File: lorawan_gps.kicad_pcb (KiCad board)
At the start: 2 copper layers, 75 x 20 mm, 60 parts, among them IC1 TPS61201, P1 BL_PAD, P10 CONN_01X01, P11 CONN_01X04, P2 SWD_DAT, P3 SWD_CLK, P4 SWD_3V3, P5 SWD_GND, P6 SWD_RST, P8 CONN_01X01, P9 CONN_01X01, SW1 SW_PUSH, SW2 SW_PUSH, U1 SHT21, U2 MPU-9250, U3 RFM9xW, U4 SAMD21E17A, U5 MAX-M8, Y1 32.768kHz

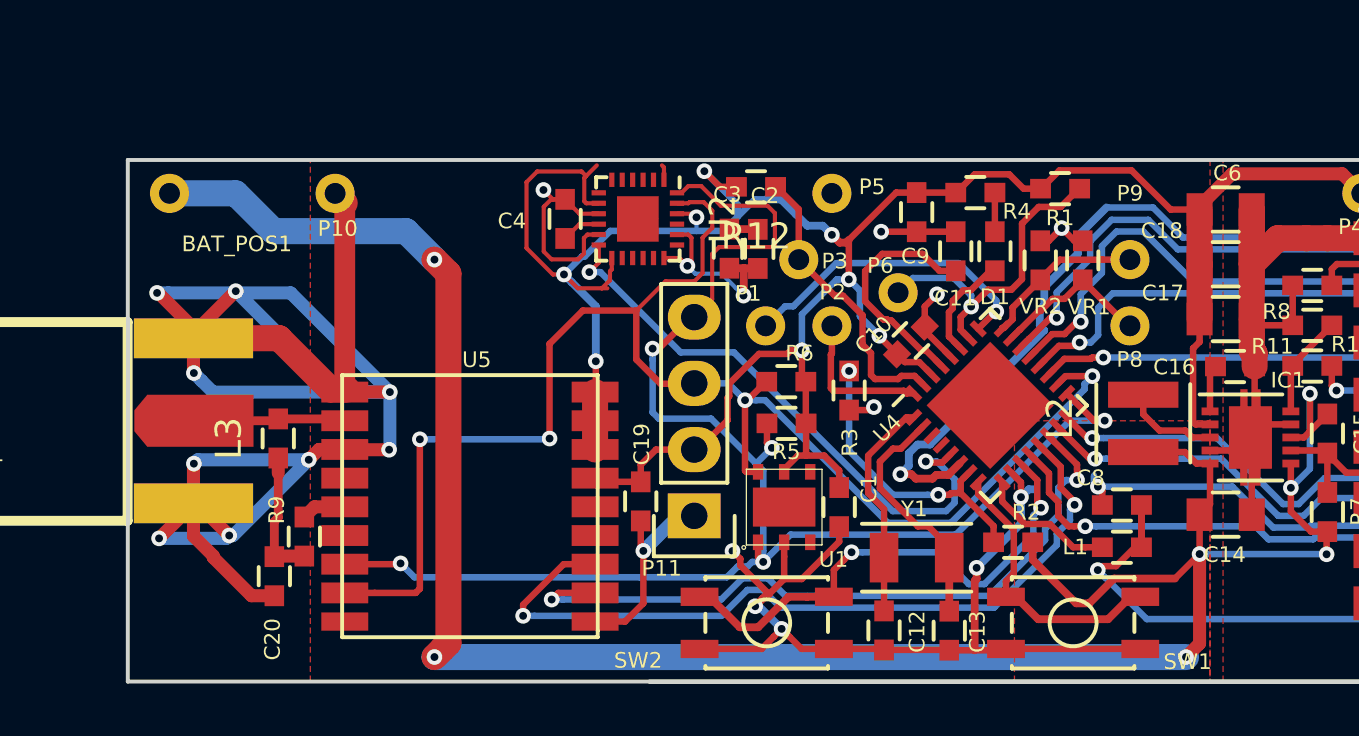
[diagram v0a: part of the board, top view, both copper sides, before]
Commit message: Started work to add the power mux and USB connector
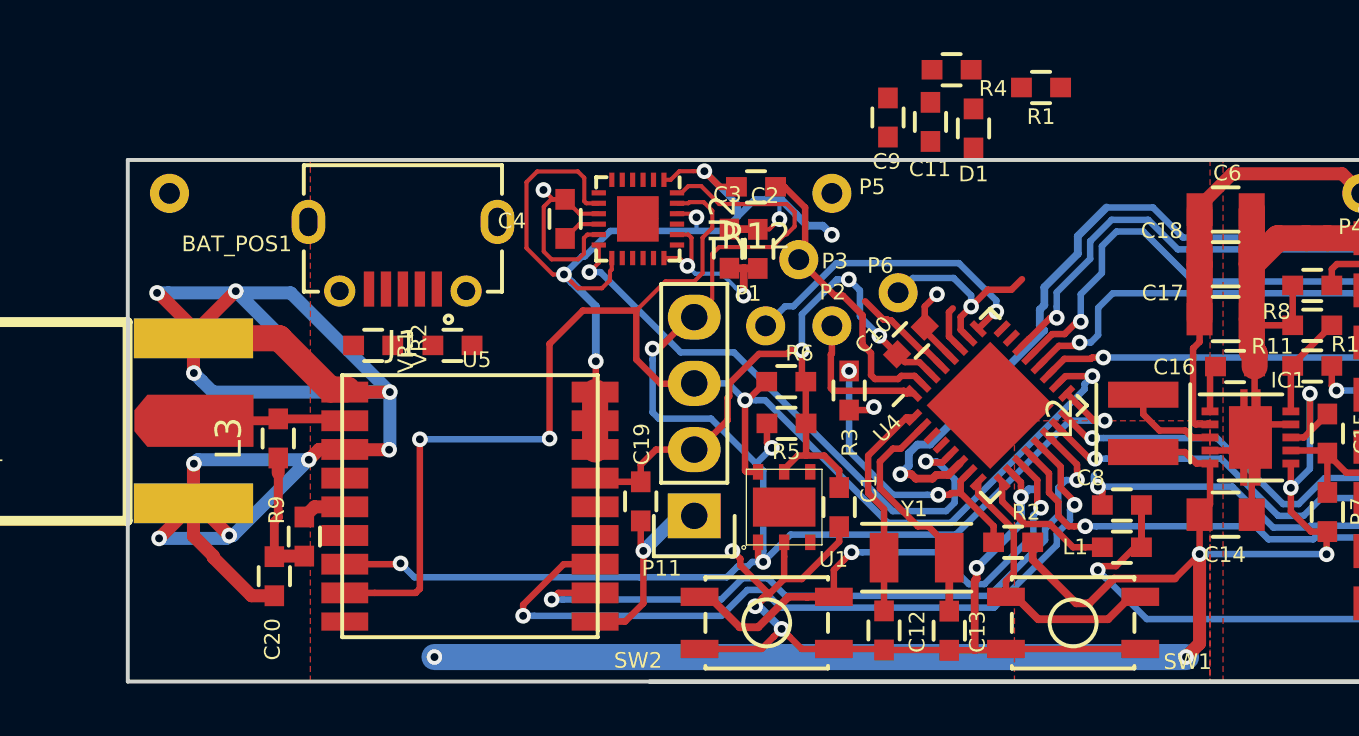
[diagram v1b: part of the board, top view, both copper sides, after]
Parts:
- removed P10, P8, P9: CONN_01X01, Measurement_Points:Measurement_Point_Round-TH_Small
- added J1: MICRO-USB, RocketScreamKicadLibrary:MICRO-USB, F.Cu at (115.5, 73.5)
- moved VR2 25.8 mm to (114.4, 77.1), turned to 180 degrees
- moved VR1 24.4 mm to (117.5, 77.1), turned to 0 degrees
- moved C11 5.05 mm to (135.8, 68.5)
- moved R4 4.80 mm to (136.6, 66.5)
- moved D1 4.78 mm to (137.4, 68.8)
- moved R1 3.95 mm to (140.0, 67.2)
- moved C9 3.79 mm to (134.2, 68.4)
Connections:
- net Net-(P8-Pad1) renamed /MCU/Data-
- net Net-(P9-Pad1) renamed /MCU/Data+
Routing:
- net /Battery/V_BAT: track 91.3 -> 64.4 mm, vias 7 -> 6
- net +3V3: track 162.6 -> 146.5 mm, vias 12 -> 13
- net GND: track 228.3 -> 215.7 mm, vias 28 -> 26
- net /MCU/Data+: track 6.30 -> 0.00 mm
- net /MCU/Data-: track 6.25 -> 0.00 mm
- net Net-(C11-Pad1): track 9.12 -> 3.95 mm
- net /MCU/#RESET: track 12.5 -> 7.63 mm
- net Net-(D1-Pad1): track 4.11 -> 1.73 mm
- net Net-(D1-Pad2): track 1.51 -> 0.00 mm
- net /MCU/MPU_SDA: track 60.8 -> 61.9 mm

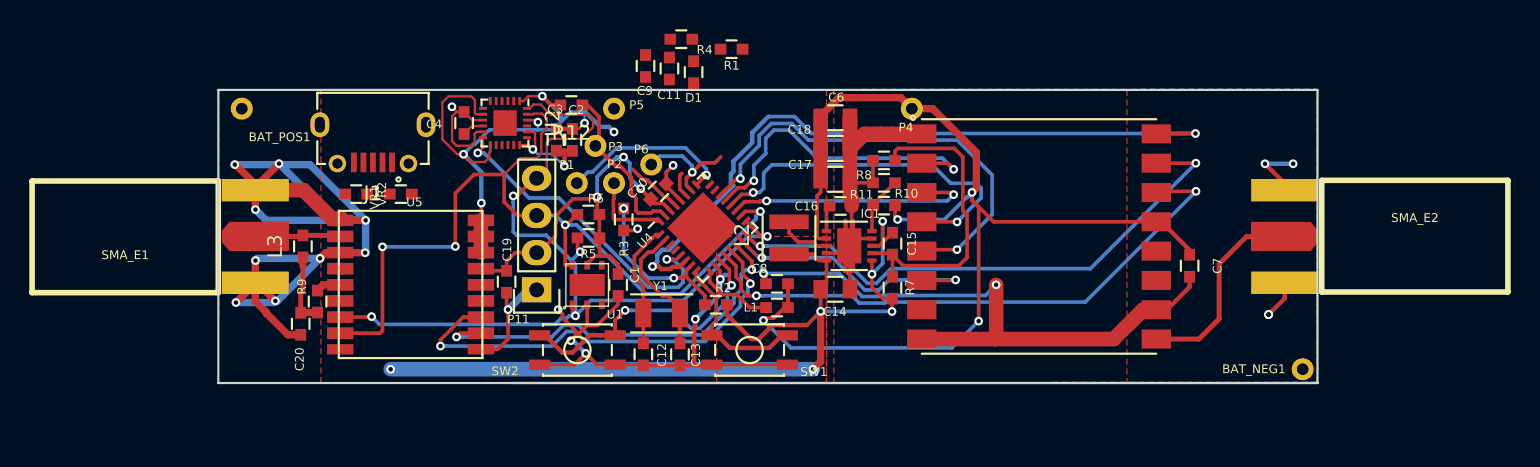
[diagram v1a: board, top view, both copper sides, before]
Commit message: Added USB connector, diode or etc to layout@
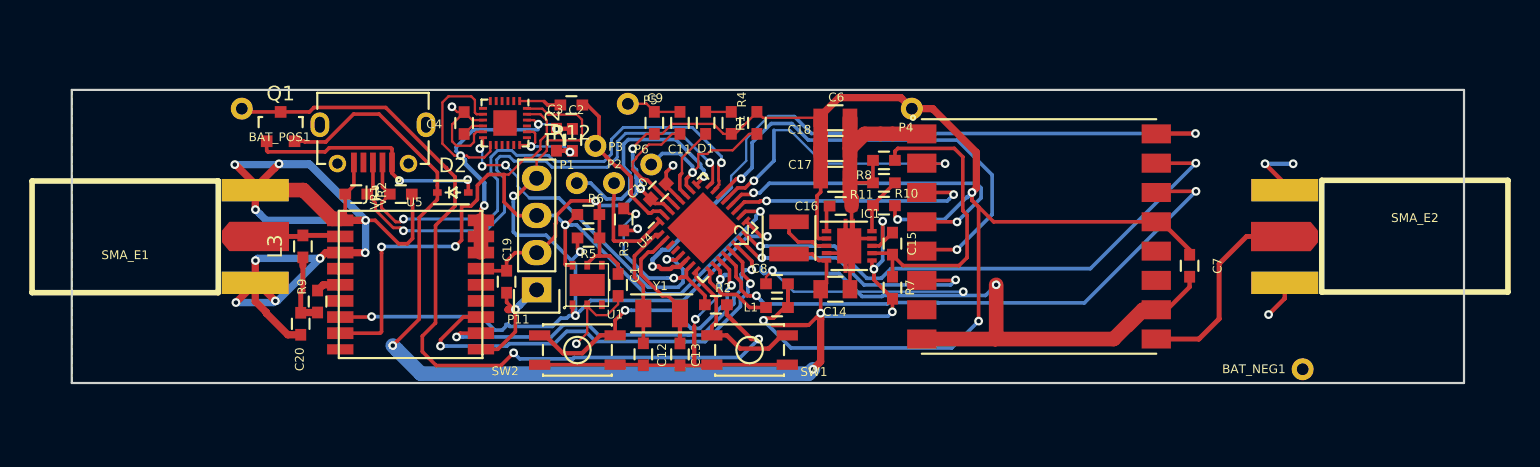
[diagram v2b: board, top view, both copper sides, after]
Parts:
- added D2: D_Schottky, Diodes_SMD:SOD-323, F.Cu at (121.0, 77.0)
- added Q1: Q_PMOS_GSD, TO_SOT_Packages_SMD:SOT-23, F.Cu at (109.2, 72.5)
- moved R4 6.65 mm to (140.0, 72.2), turned to 90 degrees
- moved R1 5.32 mm to (141.8, 72.2), turned to 270 degrees
- moved C9 3.93 mm to (134.8, 72.2), turned to 90 degrees
- moved C11 3.78 mm to (136.5, 72.2)
- moved D1 3.56 mm to (138.2, 72.2)
- moved P5 1.00 mm to (132.9, 71.0)
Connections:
- net /MCU/Data+ renamed /Battery and USB Connector/D+
- net /MCU/Data- renamed /Battery and USB Connector/D-
- BAT_POS1 pad 1: /Battery/V_BAT -> /Battery and USB Connector/V_BAT
- C14 pad 1: /Battery/V_BAT -> Net-(C14-Pad1)
- C15 pad 1: /Battery/V_BAT -> Net-(C14-Pad1)
- IC1 pad 5: /Battery/V_BAT -> Net-(C14-Pad1)
- IC1 pad 6: /Battery/V_BAT -> Net-(C14-Pad1)
- IC1 pad 8: /Battery/V_BAT -> Net-(C14-Pad1)
- J1 pad 4: Net-(J1-Pad4) -> (no net)
- J1 pad 6: GND -> (no net)
- J1 pad 7: GND -> (no net)
- J1 pad 8: GND -> (no net)
- J1 pad 9: GND -> (no net)
- L2 pad 1: /Battery/V_BAT -> Net-(C14-Pad1)
- R2 pad 1: /Battery/V_BAT -> /Battery and USB Connector/V_BAT
- R7 pad 1: /Battery/V_BAT -> Net-(C14-Pad1)
- U1 pad 3: Net-(U1-Pad3) -> (no net)
- U1 pad 4: Net-(U1-Pad4) -> (no net)
- U2 pad 14: Net-(U2-Pad14) -> (no net)
- U2 pad 15: Net-(U2-Pad15) -> (no net)
- U2 pad 16: Net-(U2-Pad16) -> (no net)
- U2 pad 17: Net-(U2-Pad17) -> (no net)
- U2 pad 19: Net-(U2-Pad19) -> (no net)
- U2 pad 2: Net-(U2-Pad2) -> (no net)
- U2 pad 21: Net-(U2-Pad21) -> (no net)
- U2 pad 3: Net-(U2-Pad3) -> (no net)
- U2 pad 4: Net-(U2-Pad4) -> (no net)
- U2 pad 5: Net-(U2-Pad5) -> (no net)
- U2 pad 6: Net-(U2-Pad6) -> (no net)
- U2 pad 7: Net-(U2-Pad7) -> (no net)
- U3 pad 11: Net-(U3-Pad11) -> (no net)
- U3 pad 12: Net-(U3-Pad12) -> (no net)
- U3 pad 7: Net-(U3-Pad7) -> (no net)
- U4 pad 3: Net-(U4-Pad3) -> (no net)
- U4 pad 4: Net-(U4-Pad4) -> (no net)
- U5 pad 13: Net-(U5-Pad13) -> (no net)
- U5 pad 15: Net-(U5-Pad15) -> (no net)
- U5 pad 18: Net-(U5-Pad18) -> (no net)
- U5 pad 4: Net-(U5-Pad4) -> (no net)
- U5 pad 5: Net-(U5-Pad5) -> (no net)
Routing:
- net Net-(C14-Pad1): track 0.00 -> 85.0 mm, vias 0 -> 6
- net /Battery/V_BAT: track 64.4 -> 0.00 mm, vias 6 -> 0
- net /Battery and USB Connector/V_BAT: track 0.00 -> 57.5 mm, vias 0 -> 2
- net /Battery and USB Connector/D-: track 0.00 -> 37.1 mm, vias 0 -> 2
- net /Battery and USB Connector/D+: track 0.00 -> 36.4 mm, vias 0 -> 2
- net GND: track 215.7 -> 239.8 mm, vias 26 -> 24
- net Net-(D2-Pad2): track 0.00 -> 17.3 mm, vias 0 -> 2
- net +3V3: track 146.5 -> 153.8 mm, vias 13 -> 11
- net Net-(C11-Pad1): track 3.95 -> 8.52 mm
- net /MCU/#RESET: track 7.63 -> 11.4 mm
- net Net-(P1-Pad1): track 11.8 -> 15.4 mm
- net Net-(D1-Pad1): track 1.73 -> 5.08 mm
- net Net-(P2-Pad1): track 5.66 -> 7.67 mm
- net Net-(D1-Pad2): track 0.00 -> 1.75 mm
- net /MCU/MPU_SCK: track 24.9 -> 23.3 mm
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- removed copper zone on F.Cu, net +3V3
- removed copper zone on F.Cu, net /Battery/V_BAT
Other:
- board size 75 x 20 mm -> 95 x 20 mm

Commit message: Added dielectric antennae, finished wiring, DRC pass, no unconnects
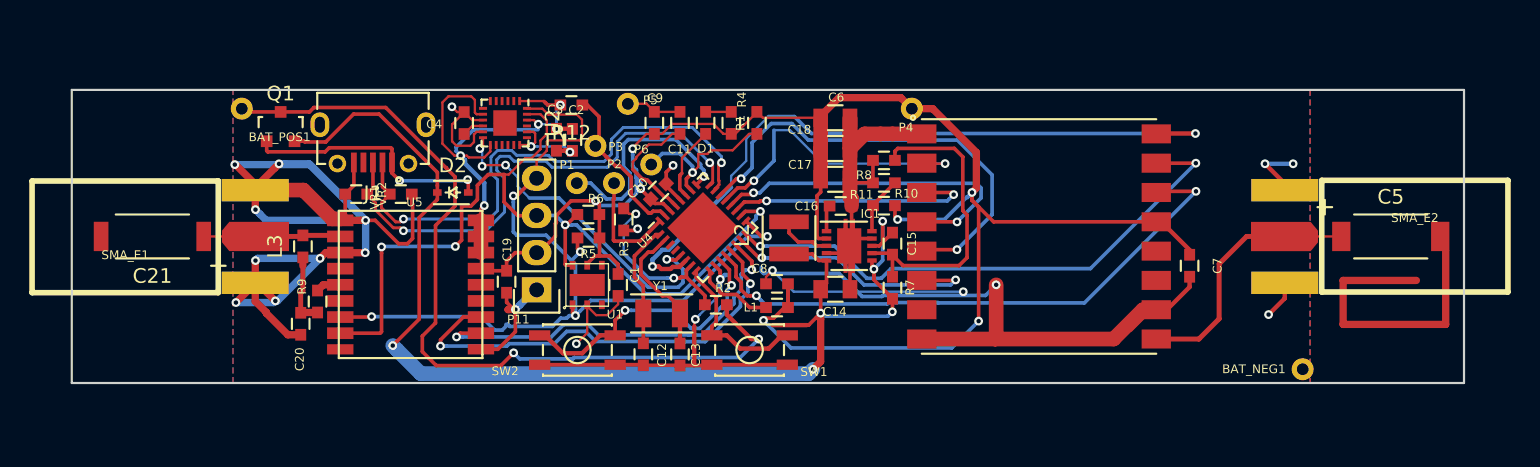
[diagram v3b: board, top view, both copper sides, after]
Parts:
- added C21: CP, Johanson:1575AT43A0040, F.Cu at (100.5, 80.0)
- added C5: CP, Johanson:0868AT43A0020, F.Cu at (185.0, 80.0)
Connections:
- J1 pad 4: (no net) -> Net-(J1-Pad4)
- J1 pad 6: (no net) -> Net-(J1-Pad6)
- J1 pad 7: (no net) -> Net-(J1-Pad7)
- J1 pad 8: (no net) -> Net-(J1-Pad8)
- J1 pad 9: (no net) -> Net-(J1-Pad9)
- U1 pad 3: (no net) -> Net-(U1-Pad3)
- U1 pad 4: (no net) -> Net-(U1-Pad4)
- U2 pad 14: (no net) -> Net-(U2-Pad14)
- U2 pad 15: (no net) -> Net-(U2-Pad15)
- U2 pad 16: (no net) -> Net-(U2-Pad16)
- U2 pad 17: (no net) -> Net-(U2-Pad17)
- U2 pad 19: (no net) -> Net-(U2-Pad19)
- U2 pad 2: (no net) -> Net-(U2-Pad2)
- U2 pad 21: (no net) -> Net-(U2-Pad21)
- U2 pad 3: (no net) -> Net-(U2-Pad3)
- U2 pad 4: (no net) -> Net-(U2-Pad4)
- U2 pad 5: (no net) -> Net-(U2-Pad5)
- U2 pad 6: (no net) -> Net-(U2-Pad6)
- U2 pad 7: (no net) -> Net-(U2-Pad7)
- U3 pad 11: (no net) -> Net-(U3-Pad11)
- U3 pad 12: (no net) -> Net-(U3-Pad12)
- U3 pad 7: (no net) -> Net-(U3-Pad7)
- U4 pad 3: (no net) -> Net-(U4-Pad3)
- U4 pad 4: (no net) -> Net-(U4-Pad4)
- U5 pad 13: (no net) -> Net-(U5-Pad13)
- U5 pad 15: (no net) -> Net-(U5-Pad15)
- U5 pad 18: (no net) -> Net-(U5-Pad18)
- U5 pad 4: (no net) -> Net-(U5-Pad4)
- U5 pad 5: (no net) -> Net-(U5-Pad5)
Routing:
- net Net-(C5-Pad1): track 15.9 -> 20.0 mm
- net +3V3: track 153.8 -> 157.6 mm, vias 11 -> 12
- net /GPS/GPS_FEEDER: track 7.88 -> 9.38 mm
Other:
- net class Default: clearance 0.2 -> 0.16; trace_width 0.25 -> 0.16
- rule trace_clearance: 0.2 -> 0.16

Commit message: Added USB monitoring resistors, still need to set values. Also added stitching vias and tried to clean up some layout
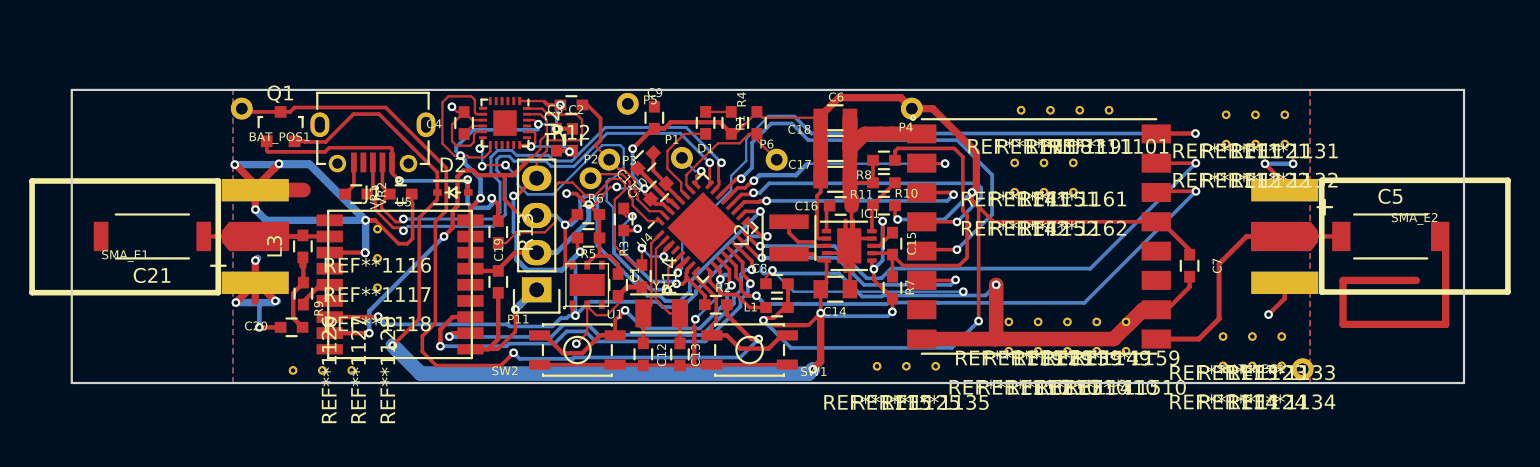
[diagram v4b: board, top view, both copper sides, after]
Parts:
- added R13: R, Capacitors_SMD:C_0603, F.Cu at (124.1, 79.7)
- added R14: R, Capacitors_SMD:C_0603, F.Cu at (133.9, 82.7)
- added REF**11101: Stitch_Via, Oddities:Stitch_Via, F.Cu at (165.8, 71.4)
- added REF**1111: Stitch_Via, Oddities:Stitch_Via, F.Cu at (173.8, 71.7)
- added REF**11110: Stitch_Via, Oddities:Stitch_Via, F.Cu at (158.9, 87.8)
- added REF**1112: Stitch_Via, Oddities:Stitch_Via, F.Cu at (173.8, 73.7)
- added REF**1113: Stitch_Via, Oddities:Stitch_Via, F.Cu at (173.6, 86.8)
- added REF**1114: Stitch_Via, Oddities:Stitch_Via, F.Cu at (173.6, 88.8)
- added REF**1115: Stitch_Via, Oddities:Stitch_Via, F.Cu at (149.9, 88.9)
- added REF**1116: Stitch_Via, Oddities:Stitch_Via, F.Cu at (115.9, 79.5)
- added REF**1117: Stitch_Via, Oddities:Stitch_Via, F.Cu at (115.9, 81.5)
- added REF**1118: Stitch_Via, Oddities:Stitch_Via, F.Cu at (115.9, 83.5)
- added REF**1119: Stitch_Via, Oddities:Stitch_Via, F.Cu at (158.9, 85.8)
- added REF**1121: Stitch_Via, Oddities:Stitch_Via, F.Cu at (175.8, 71.7)
- added REF**11210: Stitch_Via, Oddities:Stitch_Via, F.Cu at (160.9, 87.8)
- added REF**1122: Stitch_Via, Oddities:Stitch_Via, F.Cu at (175.8, 73.7)
- added REF**1123: Stitch_Via, Oddities:Stitch_Via, F.Cu at (175.6, 86.8)
- added REF**1124: Stitch_Via, Oddities:Stitch_Via, F.Cu at (175.6, 88.8)
- added REF**1125: Stitch_Via, Oddities:Stitch_Via, F.Cu at (151.9, 88.9)
- added REF**1126: Stitch_Via, Oddities:Stitch_Via, F.Cu at (110.1, 89.1)
- added REF**1127: Stitch_Via, Oddities:Stitch_Via, F.Cu at (112.1, 89.1)
- added REF**1128: Stitch_Via, Oddities:Stitch_Via, F.Cu at (114.1, 89.1)
- added REF**1129: Stitch_Via, Oddities:Stitch_Via, F.Cu at (160.9, 85.8)
- added REF**1131: Stitch_Via, Oddities:Stitch_Via, F.Cu at (177.8, 71.7)
- added REF**11310: Stitch_Via, Oddities:Stitch_Via, F.Cu at (162.9, 87.8)
- added REF**1132: Stitch_Via, Oddities:Stitch_Via, F.Cu at (177.8, 73.7)
- added REF**1133: Stitch_Via, Oddities:Stitch_Via, F.Cu at (177.6, 86.8)
- added REF**1134: Stitch_Via, Oddities:Stitch_Via, F.Cu at (177.6, 88.8)
- added REF**1135: Stitch_Via, Oddities:Stitch_Via, F.Cu at (153.9, 88.9)
- added REF**1139: Stitch_Via, Oddities:Stitch_Via, F.Cu at (162.9, 85.8)
- added REF**1141: Stitch_Via, Oddities:Stitch_Via, F.Cu at (159.3, 75.0)
- added REF**11410: Stitch_Via, Oddities:Stitch_Via, F.Cu at (164.9, 87.8)
- added REF**1142: Stitch_Via, Oddities:Stitch_Via, F.Cu at (159.3, 77.0)
- added REF**1149: Stitch_Via, Oddities:Stitch_Via, F.Cu at (164.9, 85.8)
- added REF**1151: Stitch_Via, Oddities:Stitch_Via, F.Cu at (161.3, 75.0)
- added REF**11510: Stitch_Via, Oddities:Stitch_Via, F.Cu at (166.9, 87.8)
- added REF**1152: Stitch_Via, Oddities:Stitch_Via, F.Cu at (161.3, 77.0)
- added REF**1159: Stitch_Via, Oddities:Stitch_Via, F.Cu at (166.9, 85.8)
- added REF**1161: Stitch_Via, Oddities:Stitch_Via, F.Cu at (163.3, 75.0)
- added REF**1162: Stitch_Via, Oddities:Stitch_Via, F.Cu at (163.3, 77.0)
- added REF**1171: Stitch_Via, Oddities:Stitch_Via, F.Cu at (159.8, 71.4)
- added REF**1181: Stitch_Via, Oddities:Stitch_Via, F.Cu at (161.8, 71.4)
- added REF**1191: Stitch_Via, Oddities:Stitch_Via, F.Cu at (163.8, 71.4)
- moved P6 8.57 mm to (143.1, 74.8)
- moved P1 7.38 mm to (136.6, 74.6)
- moved C11 3.50 mm to (134.2, 74.8), turned to 45 degrees
- moved P2 1.63 mm to (130.4, 76.0)
- moved P3 1.33 mm to (131.7, 74.8)
- moved R9 1.11 mm to (110.8, 83.9), turned to 270 degrees
- moved U5 0.72 mm to (117.4, 87.7)
- moved C20 0.66 mm to (110.0, 86.2), turned to 180 degrees
- moved C19 0.57 mm to (124.1, 83.1)
- moved C9 0.35 mm to (134.8, 71.9)
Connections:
- C21 pad 2: Net-(C21-Pad2) -> (no net)
- C5 pad 2: Net-(C5-Pad2) -> (no net)
- J1 pad 4: Net-(J1-Pad4) -> (no net)
- J1 pad 6: Net-(J1-Pad6) -> (no net)
- J1 pad 7: Net-(J1-Pad7) -> (no net)
- J1 pad 8: Net-(J1-Pad8) -> (no net)
- J1 pad 9: Net-(J1-Pad9) -> (no net)
- U1 pad 3: Net-(U1-Pad3) -> (no net)
- U1 pad 4: Net-(U1-Pad4) -> (no net)
- U2 pad 14: Net-(U2-Pad14) -> (no net)
- U2 pad 15: Net-(U2-Pad15) -> (no net)
- U2 pad 16: Net-(U2-Pad16) -> (no net)
- U2 pad 17: Net-(U2-Pad17) -> (no net)
- U2 pad 19: Net-(U2-Pad19) -> (no net)
- U2 pad 2: Net-(U2-Pad2) -> (no net)
- U2 pad 21: Net-(U2-Pad21) -> (no net)
- U2 pad 3: Net-(U2-Pad3) -> (no net)
- U2 pad 4: Net-(U2-Pad4) -> (no net)
- U2 pad 5: Net-(U2-Pad5) -> (no net)
- U2 pad 6: Net-(U2-Pad6) -> (no net)
- U2 pad 7: Net-(U2-Pad7) -> (no net)
- U3 pad 11: Net-(U3-Pad11) -> (no net)
- U3 pad 12: Net-(U3-Pad12) -> (no net)
- U3 pad 7: Net-(U3-Pad7) -> (no net)
- U4 pad 3: Net-(U4-Pad3) -> /Battery and USB Connector/V_USB_Sense
- U4 pad 4: Net-(U4-Pad4) -> (no net)
- U5 pad 13: Net-(U5-Pad13) -> (no net)
- U5 pad 15: Net-(U5-Pad15) -> (no net)
- U5 pad 18: Net-(U5-Pad18) -> (no net)
- U5 pad 4: Net-(U5-Pad4) -> (no net)
- U5 pad 5: Net-(U5-Pad5) -> (no net)
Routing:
- net /Battery and USB Connector/V_USB_Sense: track 0.00 -> 24.0 mm, vias 0 -> 2
- net GND: track 239.8 -> 224.8 mm
- net Net-(P1-Pad1): track 15.4 -> 2.77 mm
- net /9axis/INT_9AXIS: track 23.2 -> 29.8 mm
- net Net-(D2-Pad2): track 17.3 -> 23.0 mm, vias 2 -> 3
- net Net-(C11-Pad1): track 8.52 -> 3.67 mm
- net /MCU/MPU_SDA: track 61.0 -> 64.2 mm
- net /MCU/MPU_SCL: track 58.1 -> 61.2 mm
- net /MCU/MPU_MISO: track 20.8 -> 17.6 mm
- net +3V3: track 157.6 -> 160.7 mm, vias 12 -> 14
- net /GPS/GPS_FEEDER: track 9.38 -> 11.6 mm
- net /MCU/MPU_INT5: track 48.7 -> 46.6 mm
- net /MCU/#RESET: track 11.4 -> 9.60 mm, vias 1 -> 0
- net Net-(D1-Pad1): track 5.08 -> 6.63 mm
- net Net-(C20-Pad1): track 5.00 -> 5.91 mm
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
